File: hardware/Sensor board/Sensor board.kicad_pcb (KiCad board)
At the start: 2 copper layers, 12 parts, among them J1 Conn_01x07_Female, J2 bmp280, U1 HIH8130

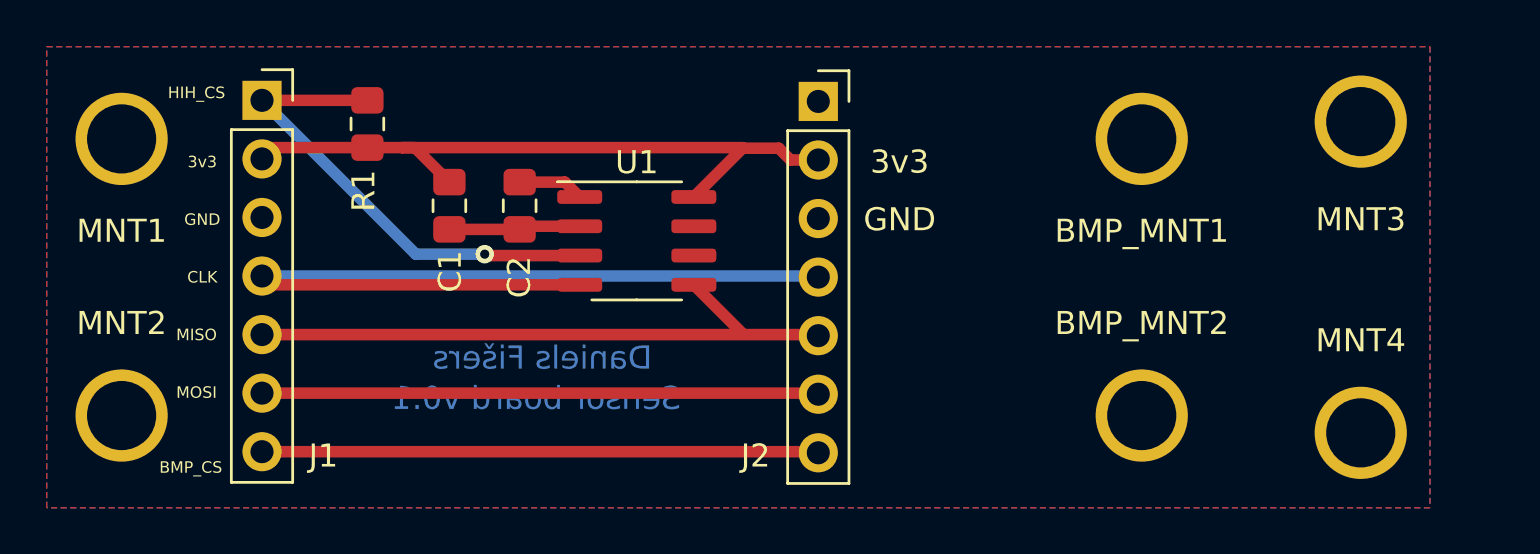
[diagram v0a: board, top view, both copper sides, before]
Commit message: Updated the footprint to fit radiation shield
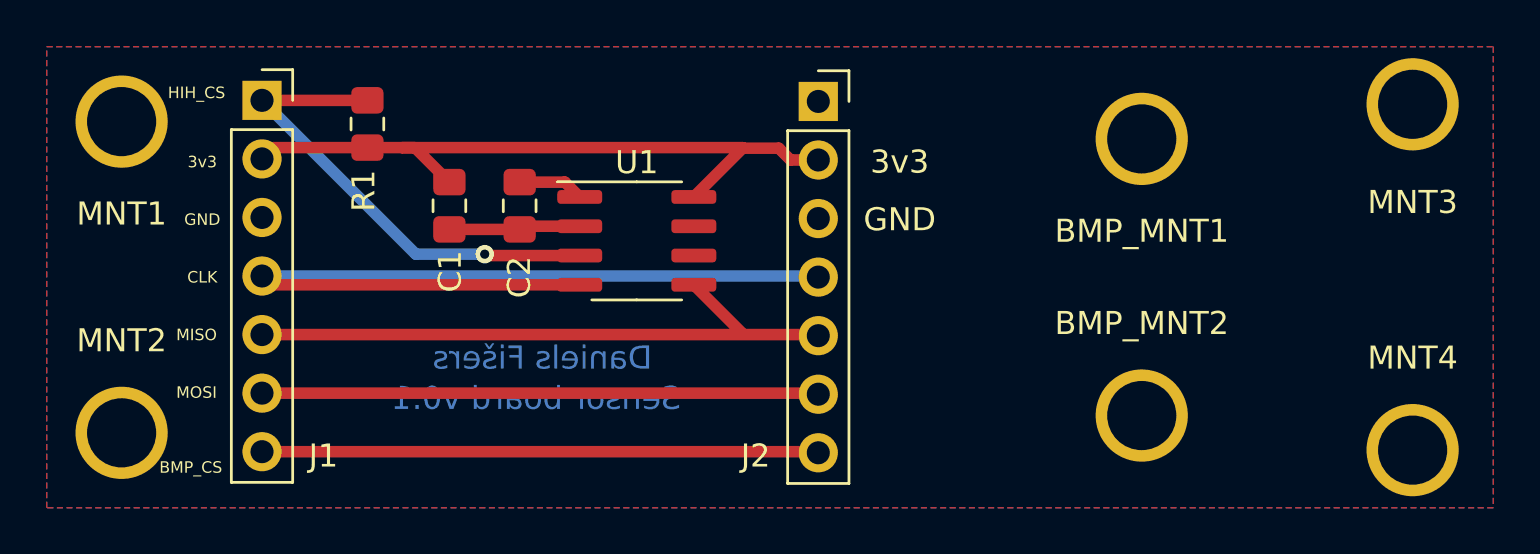
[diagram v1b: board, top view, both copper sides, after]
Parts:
- moved MNT3 2.37 mm to (103.2, 21.0)
- moved MNT4 2.37 mm to (103.2, 36.0)
- moved MNT1 0.75 mm to (47.2, 21.8)
- moved MNT2 0.75 mm to (47.2, 35.2)
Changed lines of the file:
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@@
     (solder_mask_min_width 0.25)
     (aux_axis_origin 0 0)
-    (visible_elements FFFFFF7F)
+    (visible_elements 7FFFFFFF)
     (pcbplotparams
       (layerselection 0x02000_ffffffff)
@@
   )
   (module MountingHole:MountingHole_3mm_Pad (layer F.Cu)
-    (at 101 21.75)
+    (at 103.25 21)
     (descr "Mounting Hole 3mm")
     (tags "mounting hole 3mm")
@@
   )
   (module MountingHole:MountingHole_3mm_Pad (layer F.Cu)
-    (at 101 35.25)
+    (at 103.25 36)
     (descr "Mounting Hole 3mm")
     (tags "mounting hole 3mm")
@@
   )
   (module MountingHole:MountingHole_3mm_Pad (layer F.Cu)
-    (at 47.25 34.5)
+    (at 47.25 35.25)
     (descr "Mounting Hole 3mm")
     (tags "mounting hole 3mm")
@@
   )
   (module MountingHole:MountingHole_3mm_Pad (layer F.Cu)
-    (at 47.25 22.5)
+    (at 47.25 21.75)
     (descr "Mounting Hole 3mm")
     (tags "mounting hole 3mm")
@@
     (effects (font (size 1 1) (thickness 0.15)))
   )
-  (gr_line (start 104 38.5) (end 44 38.5) (layer Margin) (width 0.15))
-  (gr_line (start 104 18.5) (end 104 38.5) (layer Margin) (width 0.15))
-  (gr_line (start 44 18.5) (end 104 18.5) (layer Margin) (width 0.15))
+  (gr_line (start 106.75 38.5) (end 44 38.5) (layer Margin) (width 0.15))
+  (gr_line (start 106.75 18.5) (end 106.75 38.5) (layer Margin) (width 0.15))
+  (gr_line (start 44 18.5) (end 106.75 18.5) (layer Margin) (width 0.15))
   (gr_line (start 44 18.5) (end 44 38.5) (layer Margin) (width 0.15))
   (segment (start 74.186 22.904) (end 74.186 22.878) (width 0.5) (layer F.Cu) (net 1))
@@
     (connect_pads (clearance 0.508))
     (min_thickness 0.254)
-    (fill yes (arc_segments 32) (thermal_gap 0.508) (thermal_bridge_width 0.508))
+    (fill (arc_segments 32) (thermal_gap 0.508) (thermal_bridge_width 0.508))
     (polygon
       (pts
-        (xy 44 18.5) (xy 104 18.5) (xy 104 38.5) (xy 44 38.5)
+        (xy 44 18.5) (xy 106.75 18.5) (xy 106.75 38.5) (xy 44 38.5)
       )
     )
@@
     (connect_pads (clearance 0.508))
     (min_thickness 0.254)
-    (fill yes (arc_segments 32) (thermal_gap 0.508) (thermal_bridge_width 0.508))
+    (fill (arc_segments 32) (thermal_gap 0.508) (thermal_bridge_width 0.508))
     (polygon
       (pts
-        (xy 44 18.5) (xy 104 18.5) (xy 104 38.5) (xy 44 38.5)
+        (xy 44 18.5) (xy 106.75 18.5) (xy 106.75 38.5) (xy 44 38.5)
       )
     )

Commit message: Slight improvements to the board
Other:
- board outline added: 62.8 x 20 mm
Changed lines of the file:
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@@
   (general
     (thickness 1.6)
-    (drawings 15)
+    (drawings 19)
     (tracks 33)
     (zones 0)
@@
     (visible_elements 7FFFFFFF)
     (pcbplotparams
-      (layerselection 0x02000_ffffffff)
+      (layerselection 0x010f0_ffffffff)
       (usegerberextensions false)
       (usegerberattributes false)
@@
     )
   )
+  (gr_line (start 44 38.5) (end 44 18.5) (layer Edge.Cuts) (width 0.05))
+  (gr_line (start 106.75 38.5) (end 44 38.5) (layer Edge.Cuts) (width 0.05))
+  (gr_line (start 106.75 18.5) (end 106.75 38.5) (layer Edge.Cuts) (width 0.05))
+  (gr_line (start 44 18.5) (end 106.75 18.5) (layer Edge.Cuts) (width 0.05))
   (gr_text GND (at 81 26) (layer F.SilkS)
     (effects (font (size 1 1) (thickness 0.15)))
@@
     (connect_pads (clearance 0.508))
     (min_thickness 0.254)
-    (fill (arc_segments 32) (thermal_gap 0.508) (thermal_bridge_width 0.508))
+    (fill yes (arc_segments 32) (thermal_gap 0.508) (thermal_bridge_width 0.508))
     (polygon
       (pts
@@
     (connect_pads (clearance 0.508))
     (min_thickness 0.254)
-    (fill (arc_segments 32) (thermal_gap 0.508) (thermal_bridge_width 0.508))
+    (fill yes (arc_segments 32) (thermal_gap 0.508) (thermal_bridge_width 0.508))
     (polygon
       (pts
